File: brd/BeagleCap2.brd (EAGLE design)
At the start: 75.5 x 152 mm, 35 parts, among them IC2 7805TV, J2 DS18B20, J3 Battery, U1 DHT22, X1 Conn BNC : pH, X2 Conn BNC : Dissolved Oxygen, X3 Conn BNC : Conductivity, X4 Conn BNC : ORP

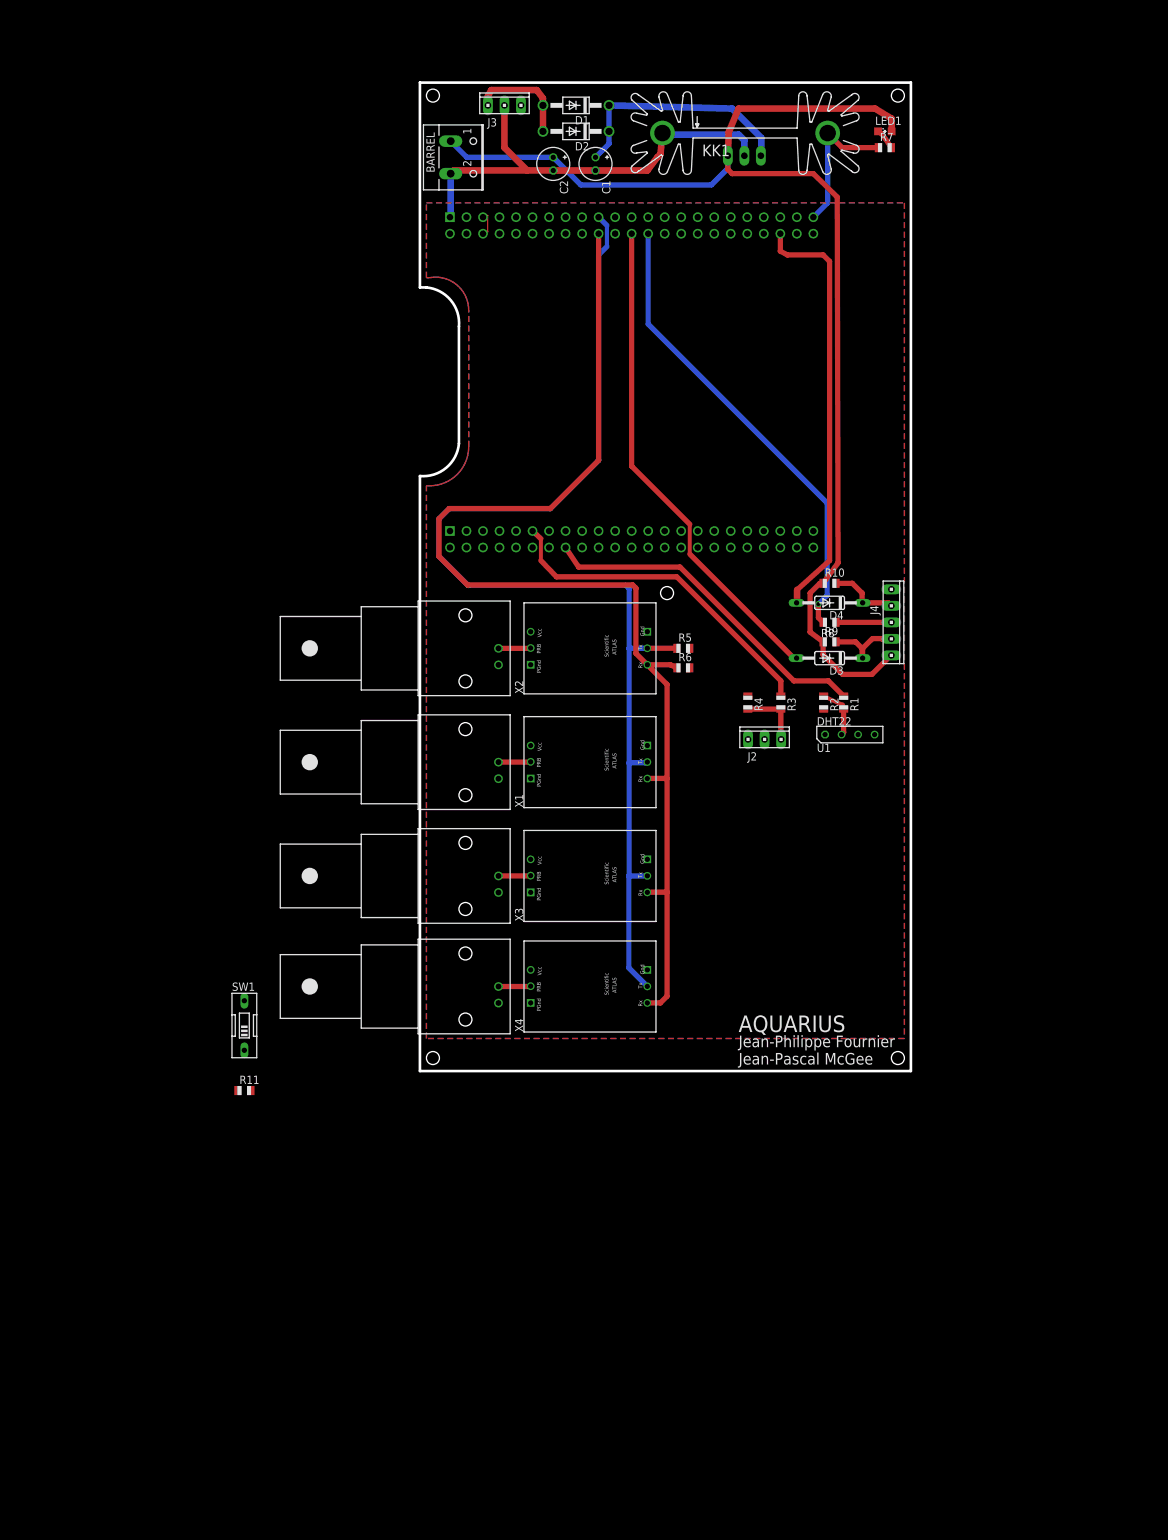
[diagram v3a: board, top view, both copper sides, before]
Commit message: Updated schematic
Added:
RTC
Logic for power management
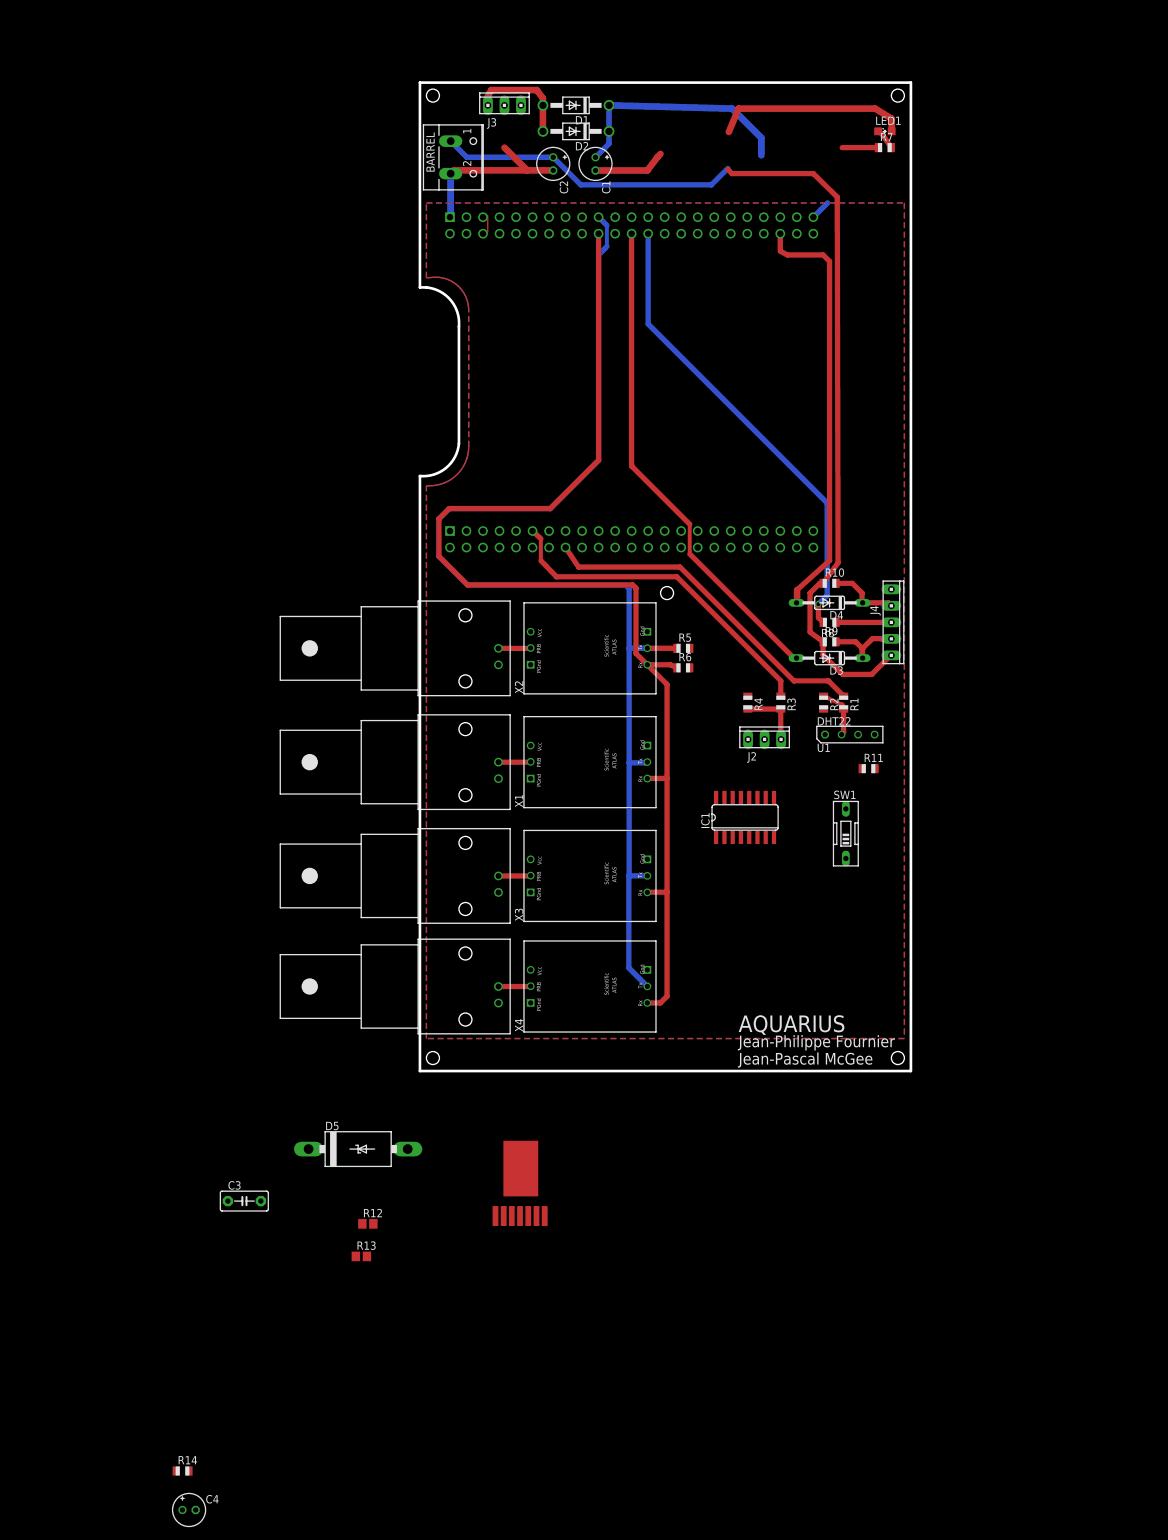
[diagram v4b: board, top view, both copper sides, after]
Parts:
- removed IC2: 7805TV, linear:TO220V
- removed KK1: SK104-PAD, heatsink:SK104-PAD
- added C3: 0.47uF, capacitor-wima:C5B3
- added C4: 10uF, rcl:E2-5
- added D5: (no value), diode:C4111-15
- added IC1: 74123D, 74xx-us:SO16
- added R12: 5.62K, resistor:R0805
- added R13: 1.07K, resistor:R0805
- added R14: 110K, adafruit:R0805
- added U$6: LMZ23605, Aquarius:TO-PMOD7
- C1: value 1uF -> 22uF
- moved R11 108.0 mm to (31.0, -27.0)
- moved SW1 97.1 mm to (27.5, -37.0)
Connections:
- new net AGND: C1.-, C3.2, J3.2, U$6.AGND, U$6.PGND, U$6.SYNC
- new net N$13: R12.1, R13.2, U$6.FB
- new net N$14: C3.1, U$6.SS/TRK
- new net VOUT: D5.A, U$6.VOUT
- net 5V: now also IC1.16, U$1.51; no longer IC2.3
- net GND: now also IC1.8; no longer C1.-, IC2.2, J3.2, KK1.K1, KK1.K2
- net VDD_5V: no longer U$1.51
- net VIN: now also U$6.VIN; no longer IC2.1
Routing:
- net GND: track 93.1 -> 36.3 mm
- net AGND: track 0.00 -> 11.2 mm
- net 5V: track 188.8 -> 181.1 mm
- net VDD_5V: track 4.08 -> 3.31 mm

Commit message: Modification au makefile du DHT22 et autre modifs
Sur le board
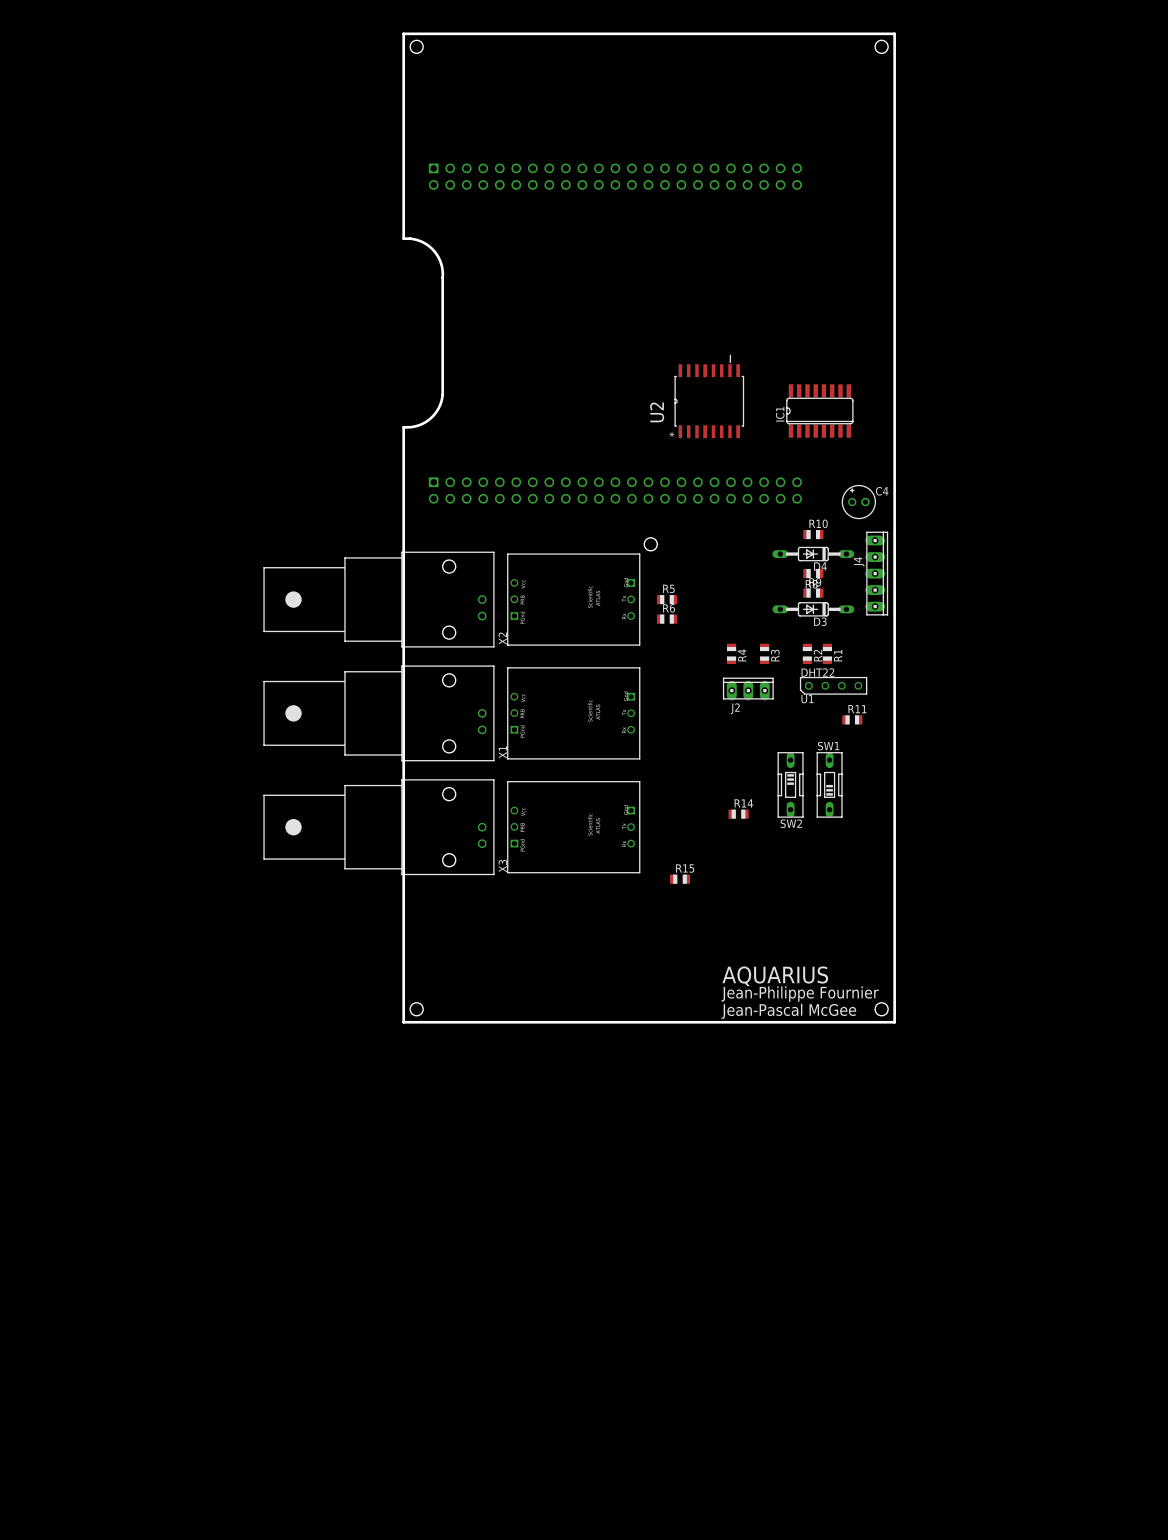
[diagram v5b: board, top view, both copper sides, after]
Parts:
- removed BARREL: (no value), con-wago-500:W237-102
- removed C1: 22uF, rcl:E2-5
- removed C2: 10uF, rcl:E2-5
- removed C3: 0.47uF, capacitor-wima:C5B3
- removed D1, D2: 1N4007, diode:DO41-10
- removed D5: (no value), diode:C4111-15
- removed J3: Battery, con-amp:10X03MTA
- removed LED1: (no value), led:SML0805
- removed R12: 5.62K, resistor:R0805
- removed R13: 1.07K, resistor:R0805
- removed R7: 330, adafruit:R0805
- removed U$5: ATLAS_STAMP, LEDscape:ATLAS_STAMP
- removed U$6: LMZ23605, Aquarius:TO-PMOD7
- removed X4: Conn BNC : ORP, con-coax:AMP_227161
- added R15: 4.7K, adafruit:R0805
- added SW2: (no value), special:EDG-01
- added U2: DS3231SN, Maxim_By_element14_Batch_1:SOIC127P1032X265-16N
- moved C4 186.1 mm to (29.5, 14.0)
- moved R14 132.3 mm to (11.0, -34.0)
- moved IC1 63.5 mm to (23.5, 28.0)
- moved U1 7.91 mm to (25.6, -14.3)
- moved D3 7.91 mm to (22.5, -2.50)
- moved D4 7.91 mm to (22.5, 6.00)
- moved J2 7.91 mm to (12.5, -15.0)
- moved J4 7.91 mm to (32.0, 3.00)
- moved R1 7.91 mm to (24.7, -9.34)
- moved R10 7.91 mm to (22.5, 9.00)
- moved R11 7.91 mm to (28.5, -19.5)
- moved R2 7.91 mm to (21.6, -9.34)
- moved R3 7.91 mm to (15.0, -9.34)
- moved R4 7.91 mm to (9.92, -9.34)
- moved R5 7.91 mm to (0.00, -1.00)
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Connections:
- net VDD_5V renamed N$1
- removed net AGND: C1.-, C3.2, J3.2, U$6.AGND, U$6.PGND, U$6.SYNC
- removed net N$1 (its old number): D1.A, D2.A, J3.3
- removed net N$13: R12.1, R13.2, U$6.FB
- removed net N$14: C3.1, U$6.SS/TRK
- removed net N$2: LED1.C, R7.2
- removed net ORP_SENSOR: U$5.PRB, X4.1
- removed net VDD_3V3EXP: U$1.49
- removed net VIN: C1.+, D1.C, D2.C, U$6.VIN
- removed net VOUT: D5.A, U$6.VOUT
- new net INT: IC1.1, R15.2, U2.3
- new net N$12: U2.4
- new net N$17: C4.+, IC1.15, R14.2
- new net N$20: IC1.13
- new net PWR_BUT: IC1.4, SW2.1, U$1.55
- net 3.3V: now also U$1.49; no longer U$5.VCC
- net 5V: now also IC1.2, IC1.3, R14.1, R15.1, U2.2; no longer BARREL.1, C2.+, LED1.A
- net GND: now also C4.-, IC1.14, SW2.2, U2.10, U2.11, U2.12, U2.13, U2.14, U2.5, U2.6, U2.7, U2.8, U2.9; no longer BARREL.2, C2.-, R7.1, U$5.GND, U$5.PGND, X4.2
- net I2C2_SCL: now also U2.16; no longer U$5.TX
- net I2C2_SDA: now also U2.15; no longer U$5.RX
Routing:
- net 5V: track 181.1 -> 0.00 mm
- net I2C2_SDA: track 180.1 -> 0.00 mm
- net I2C2_SCL: track 179.2 -> 0.00 mm
- net TX: track 76.0 -> 0.00 mm
- net RX: track 72.0 -> 0.00 mm, vias 1 -> 0
- net P: track 65.6 -> 0.00 mm
- net N$6: track 52.6 -> 0.00 mm
- net N$4: track 52.0 -> 0.00 mm
- net VIN: track 36.8 -> 0.00 mm
- net GND: track 36.3 -> 0.00 mm
- net N$1 (its old number): track 16.2 -> 0.00 mm
- net N$9: track 12.5 -> 0.00 mm
- net AGND: track 11.2 -> 0.00 mm
- net N$11: track 10.8 -> 0.00 mm
- net N$5: track 9.78 -> 0.00 mm
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- removed copper zone on layer 1, net 3.3V
- removed copper zone on layer 16, net GND
